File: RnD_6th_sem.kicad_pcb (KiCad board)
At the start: 2 copper layers, 62 x 69.1 mm, 82 parts, among them IC1 2EDF7275KXUMA1, J1 HVDC, J10 MMCX-J-P-H-ST-TH1, J2 PWM, J3 HVDC, J4 Conn_02x03_Odd_Even, J5 5V, J6 5V, J7 GND, J8 GND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

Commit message: updated the SLDO conn.
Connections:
- IC1 pad 4: GND -> unconnected-(IC1-SLDON-Pad4)
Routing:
- net GND: track 0.00 -> 1.22 mm
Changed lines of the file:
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@@
   (net 34 "Net-(J2-Pin_3)")
   (net 35 "Net-(Q2-G)")
+  (net 36 "unconnected-(IC1-SLDON-Pad4)")
   (footprint "LED_SMD:LED_0805_2012Metric" (layer "F.Cu")
     (at 124.525 58.31 180)
@@
       (net 22 "PWM2") (pinfunction "INB") (pintype "passive") (solder_mask_margin 0.1016) (zone_connect 2))
     (pad "4" smd rect (at -2.075 0 270) (size 0.8 0.35) (layers "F.Cu" "F.Mask")
-      (net 1 "GND") (pinfunction "SLDON") (pintype "passive") (solder_mask_margin 0.1016) (zone_connect 2))
+      (net 36 "unconnected-(IC1-SLDON-Pad4)") (pinfunction "SLDON") (pintype "passive+no_connect") (solder_mask_margin 0.1016) (zone_connect 2))
     (pad "5" smd rect (at -2.075 0.65 270) (size 0.8 0.35) (layers "F.Cu" "F.Mask")
       (net 1 "GND") (pinfunction "DISABLE") (pintype "passive") (solder_mask_margin 0.1016) (zone_connect 2))
@@
     (style (thickness 0.15) (arrow_length 1.27) (text_position_mode 0) (extension_height 0.58642) (extension_offset 0.5) keep_text_aligned)
   )
+  (segment (start 138.0425 63.5725) (end 138.18 63.71) (width 0.3) (layer "F.Cu") (net 1))
+  (segment (start 138.0425 62.545) (end 138.0425 63.5725) (width 0.3) (layer "F.Cu") (net 1))
   (segment (start 131.73 62.46) (end 115.95 62.46) (width 0.3) (layer "F.Cu") (net 2))
   (segment (start 132.53 63.26) (end 131.73 62.46) (width 0.3) (layer "F.Cu") (net 2))

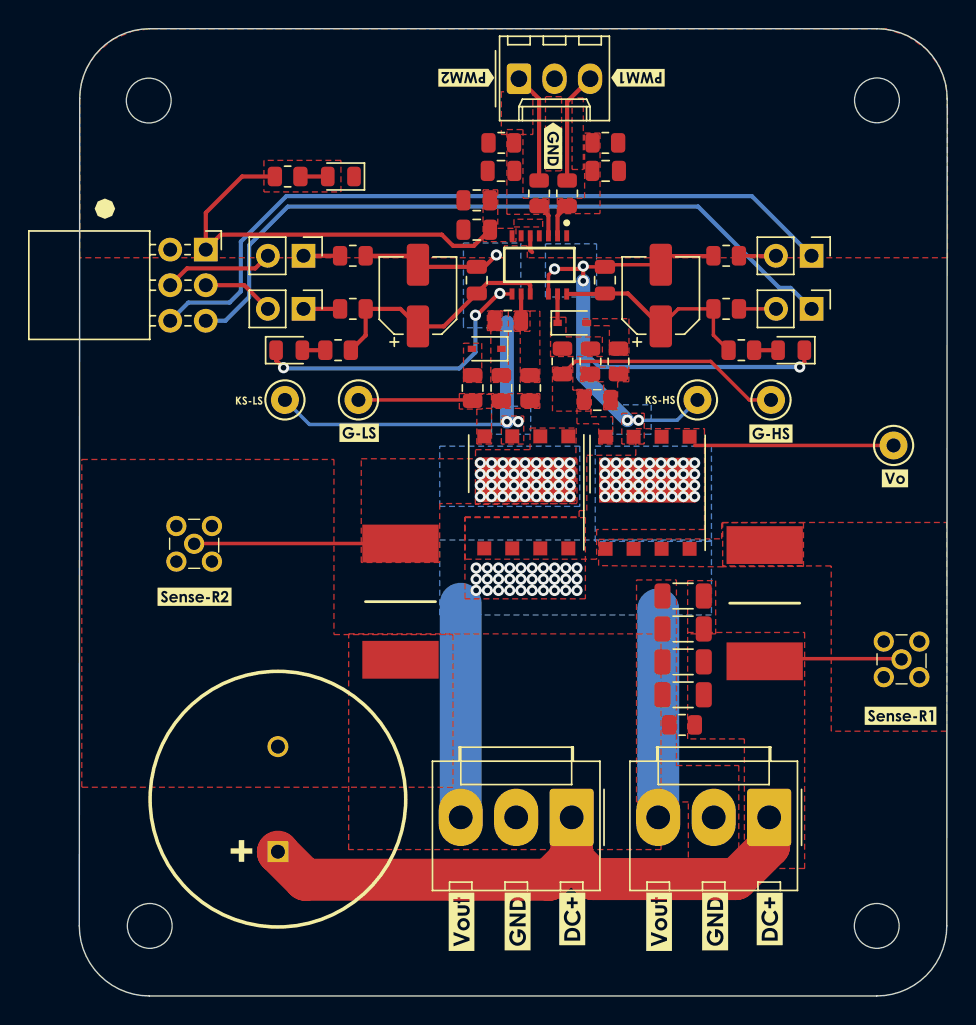
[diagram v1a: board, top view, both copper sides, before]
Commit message: changed TPs location
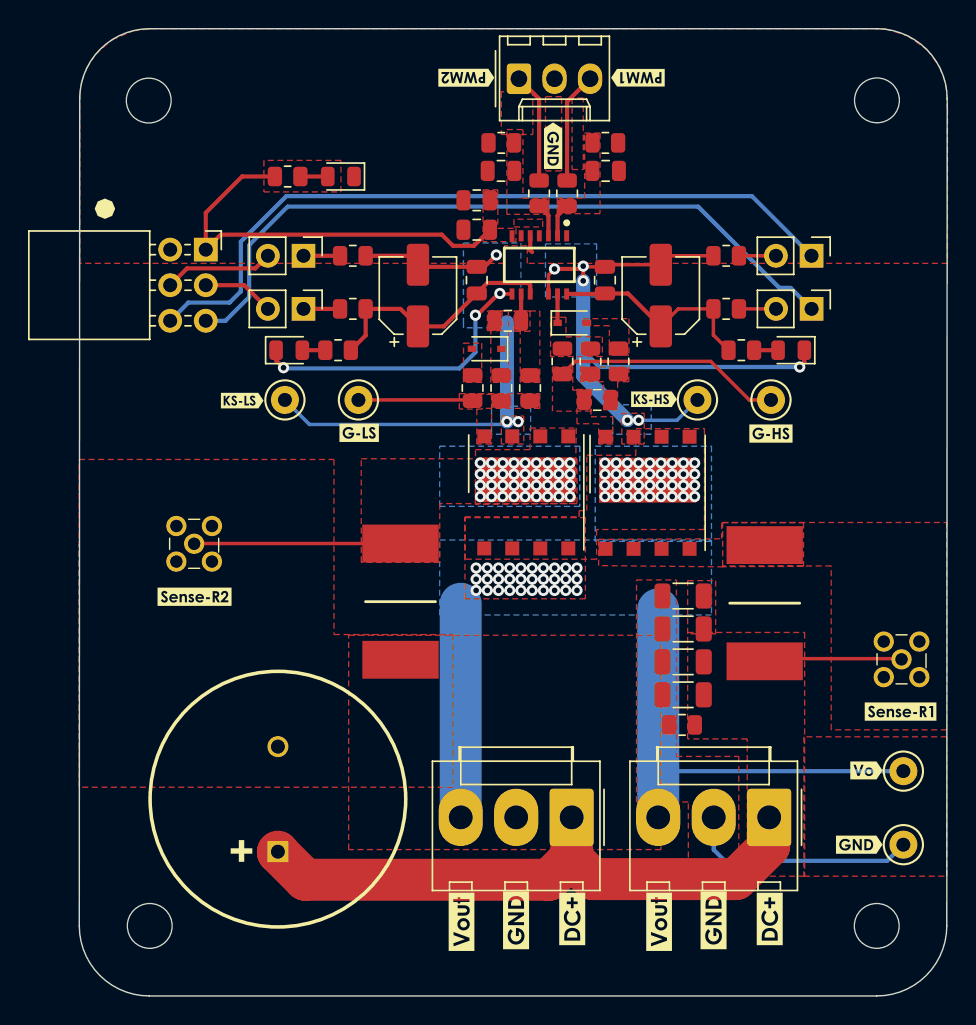
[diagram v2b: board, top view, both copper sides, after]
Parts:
- removed kibuzzard-63EDD756: G***, kibuzzard-63EDD756
- removed kibuzzard-63EE9059 (x2): G***, kibuzzard-63EE9059
- removed kibuzzard-63FF1AED: G***, kibuzzard-63FF1AED
- removed kibuzzard-63FF1AF8: G***, kibuzzard-63FF1AF8
- added TP6: TestPoint_Alt, TestPoint:TestPoint_Keystone_5000-5004_Miniature, F.Cu at (164.7, 106.0)
- added kibuzzard-640A14F1: G***, kibuzzard-640A14F1, F.Cu at (162.0, 100.7)
- added kibuzzard-640A15A1: G***, kibuzzard-640A15A1, F.Cu at (161.5, 106.0)
- added kibuzzard-640A15B0: G***, kibuzzard-640A15B0, F.Cu at (151.1, 111.4)
- added kibuzzard-640A15B9: G***, kibuzzard-640A15B9, F.Cu at (137.0, 111.4)
- added kibuzzard-640A1BB7: G***, kibuzzard-640A1BB7, F.Cu at (146.9, 74.2)
- added kibuzzard-640A1BC5: G***, kibuzzard-640A1BC5, F.Cu at (117.5, 74.3)
- moved TP4 23.3 mm to (164.7, 100.8)
- moved kibuzzard-63EDD791 0.30 mm to (164.5, 96.5)
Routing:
- net GND3: track 0.00 -> 16.7 mm
- net Net-(J1-Pin_3): track 44.3 -> 47.6 mm

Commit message: added logo
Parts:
- added G***: LOGO, logo:IITDh logo, F.Cu at (129.9, 49.8)
- added G***: LOGO, logo:IITDh logo, F.Cu at (113.9, 49.8)
- added kibuzzard-640AA404: G***, kibuzzard-640AA404, F.Cu at (121.8, 49.8)
- added kibuzzard-640AA4D3: G***, kibuzzard-640AA4D3, F.Cu at (121.8, 52.4)

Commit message: changed cap values
PWM RC filter caps changed from 100nF to 0.1nF because of limitations
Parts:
- C13, C14: value 100nF -> 0.1n
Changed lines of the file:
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@@
         (effects (font (size 1 1) (thickness 0.15)))
     )
-    (fp_text value "100nF" (at 0 1.68) (layer "F.Fab")
+    (fp_text value "0.1n" (at 0 1.68) (layer "F.Fab")
         (effects (font (size 1 1) (thickness 0.15)))
     )
@@
         (effects (font (size 1 1) (thickness 0.15)))
     )
-    (fp_text value "100nF" (at 0 1.68) (layer "F.Fab")
-        (effects (font (size 1 1) (thickness 0.15)))
-    )
+    (fp_text value "0.1n" (at 0 1.68) (layer "F.Fab")
+        (effects (font (size 1 1) (thickness 0.15)))
+    )
